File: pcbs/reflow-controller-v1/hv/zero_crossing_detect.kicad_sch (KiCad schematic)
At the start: 13 parts, among them Q1601 MMBT3904, Q1602 140357145200

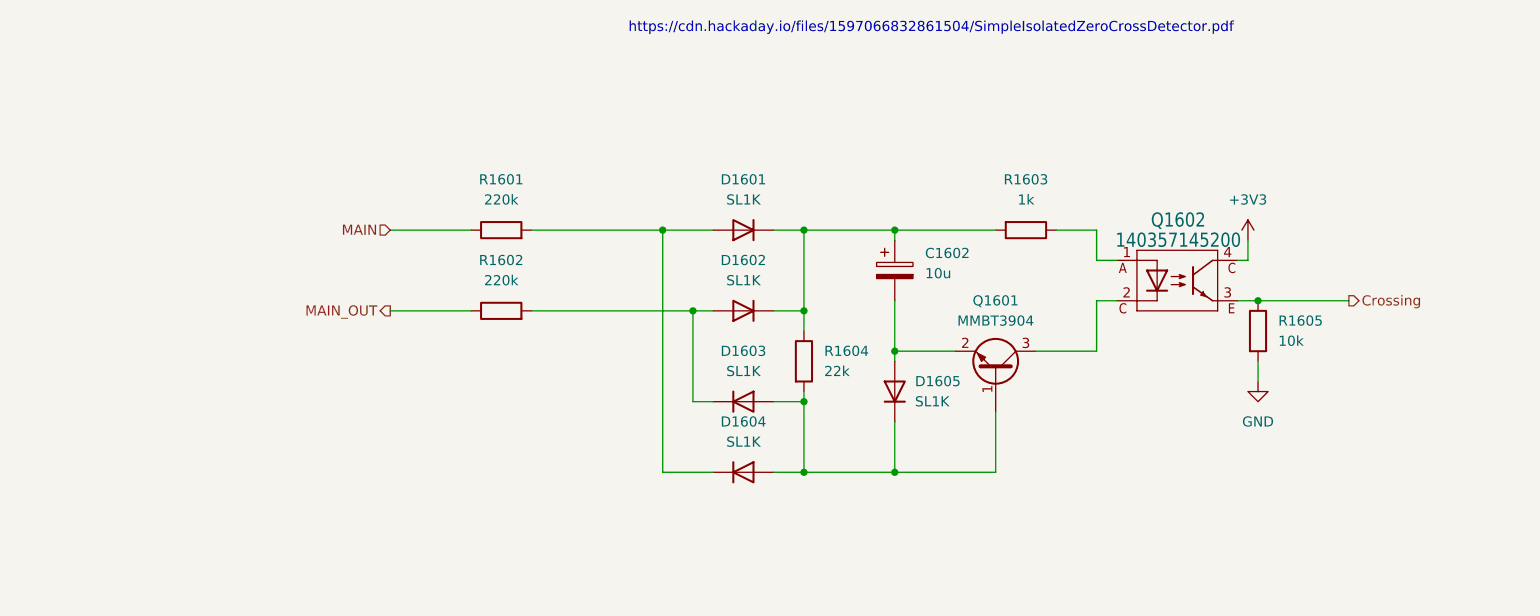
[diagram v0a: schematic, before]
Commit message: split pcbs into two for safety
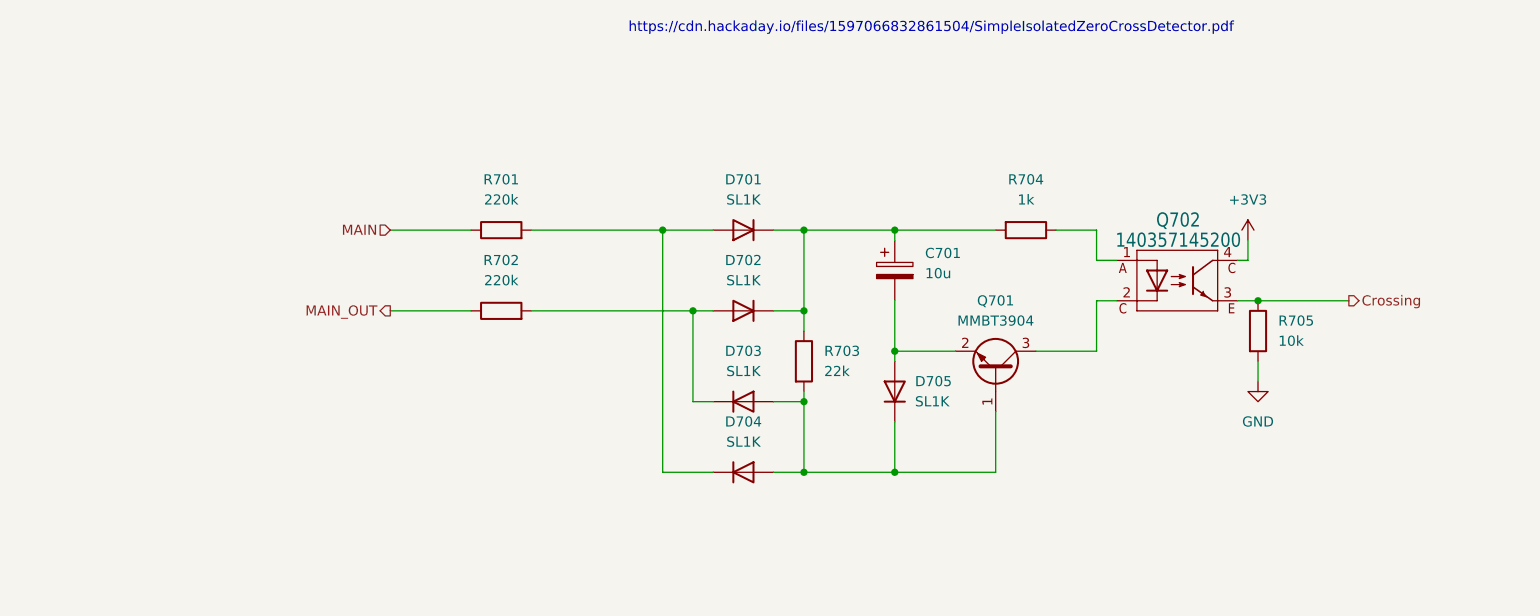
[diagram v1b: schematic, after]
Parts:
- Q702: renamed from Q1602; footprint WL-OCPT_LSOP4 -> wuerth:WL-OCPT_SOP4
- renumbered C1602 to C701, D1601 to D701, D1602 to D702, D1603 to D703, D1604 to D704, D1605 to D705, Q1601 to Q701, R1601 to R701, R1602 to R702, R1604 to R703, R1603 to R704, R1605 to R705

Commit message: Initial hv placing
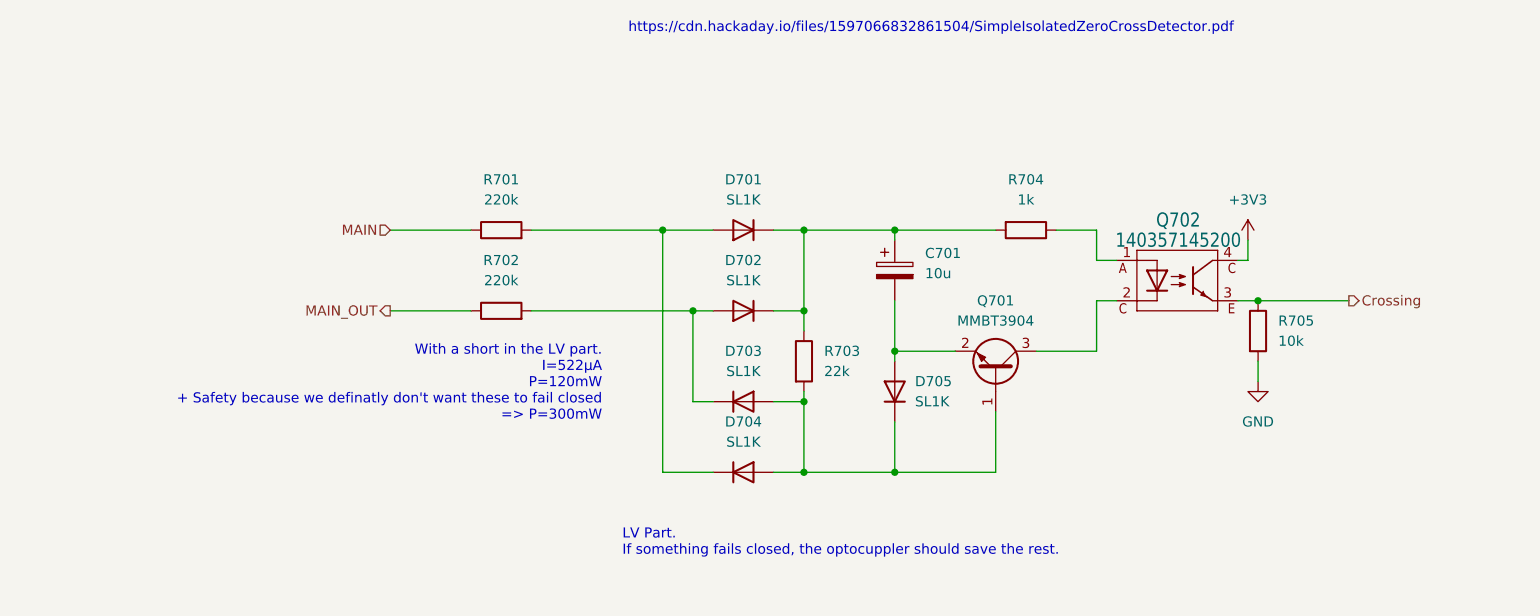
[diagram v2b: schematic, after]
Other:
- note added: "LV Part. If something fails closed, the optocuppler should save the rest."
- note added: "With a short in the LV part. I=522μA P=120mW + Safety because we definatly don't want these to fail closed => P=300mW"
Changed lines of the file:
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@@
+		)
+	)
+	(text "LV Part. \nIf something fails closed, the optocuppler should save the rest.\n"
+		(exclude_from_sim no)
+		(at 78.74 81.28 0)
+		(effects
+			(font
+				(size 1.27 1.27)
+			)
+			(justify left)
+		)
+	)
+	(text "With a short in the LV part.\nI=522μA\nP=120mW\n+ Safety because we definatly don't want these to fail closed\n=> P=300mW\n"
+		(exclude_from_sim no)
+		(at 76.2 61.214 0)
+		(effects
+			(font
+				(size 1.27 1.27)
+			)
+			(justify right)
 		)
 	)
@@
 		)
 	)
+	(rule_area
+		(polyline
+			(pts
+				(xy 78.74 33.02) (xy 78.74 77.47) (xy 137.16 77.47) (xy 137.16 33.02)
+			)
+			(stroke
+				(width 0)
+				(type dash)
+			)
+			(fill
+				(type none)
+			)
+		)
+	)
+	(netclass_flag ""
+		(length 2.54)
+		(shape round)
+		(at 97.79 33.02 0)
+		(fields_autoplaced yes)
+		(effects
+			(font
+				(size 1.27 1.27)
+			)
+			(justify left bottom)
+		)
+		(property "Netclass" "LV"
+			(at 98.4885 30.48 0)
+			(effects
+				(font
+					(size 1.27 1.27)
+				)
+				(justify left)
+			)
+		)
+		(property "Component Class" ""
+			(at -46.99 0 0)
+			(effects
+				(font
+					(size 1.27 1.27)
+					(italic yes)
+				)
+			)
+		)
+	)

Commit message: improve component selection
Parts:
- removed D702, D703, D704, D705: SL1K, Diode_SMD:D_SOD-123F, symbol Device:D
- added D706: BAS3007A-RPP, Package_TO_SOT_SMD:SOT-143, symbol Diode_Bridge:B40C2300-1500A
- C701: Order (none) -> Würth 865230440002
- D701: value SL1K -> BAS21J; footprint Diode_SMD:D_SOD-123F -> Diode_SMD:D_SOD-323F
- R701, R702: Order (none) -> Würth 560112132017
- R703, R704, R705: footprint Resistor_SMD:R_0603_1608Metric -> Resistor_SMD:R_0402_1005Metric
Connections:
- net at R702.2: now also D706.2
- net at C701.1, R703.1, R704.2: now also D706.4 (+); no longer D701.1 (K)
- net at Q701.1 (B), R703.2: now also D701.1 (K), D706.1 (-)
- net at C701.2, Q701.2 (E): now also D701.2 (A)
- net at R701.2: now also D706.3; no longer D701.2 (A)
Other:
- note added: "With just the voltage devider Resistors I=497μA P=110μW + Safety because we definatly don't want these to fail closed => P=200mW Per Resistor 5% Smaller values result in ~524μA 5% Tollerance should be fine"
- note removed: "With a short in the LV part. I=522μA P=120mW + Safety because we definatly don't want these to fail closed => P=300mW"
- moved on the sheet: C701, Q701, Q702, R701, R702, R703, R704, R705

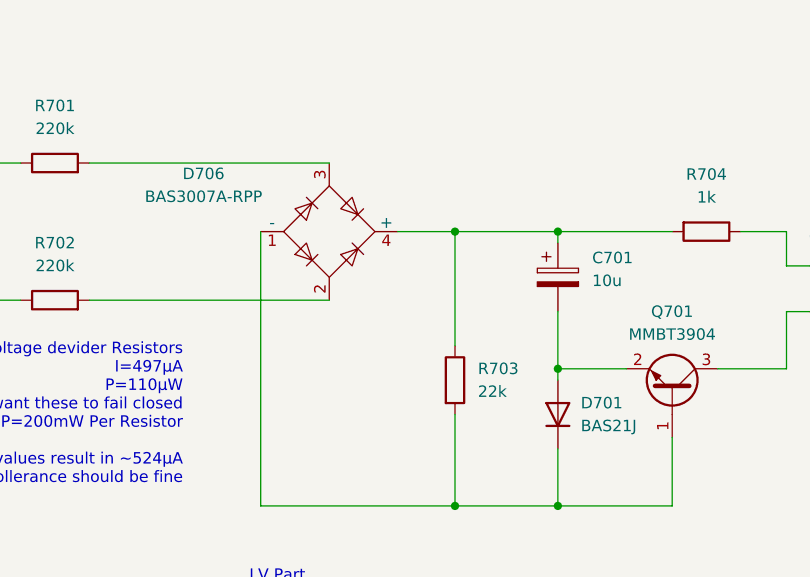
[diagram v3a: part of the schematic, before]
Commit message: route hv pcb
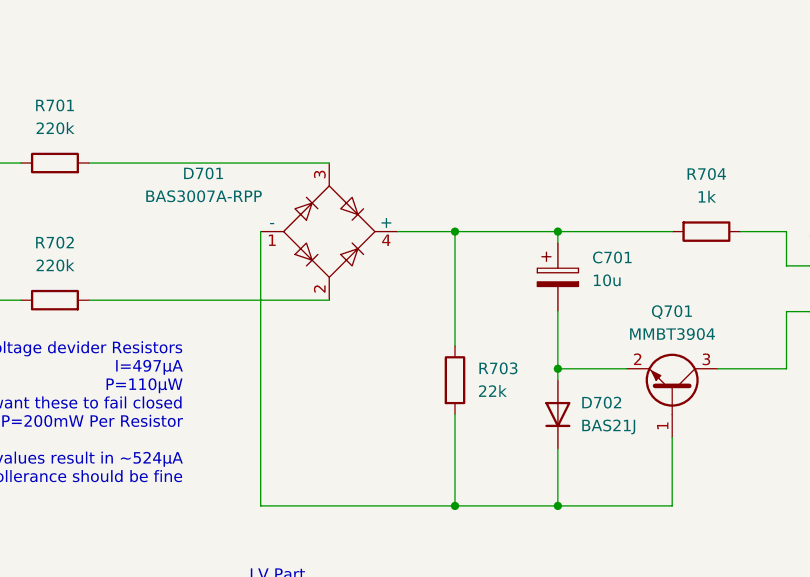
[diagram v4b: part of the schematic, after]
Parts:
- renumbered D706 to D701, D701 to D702
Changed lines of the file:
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@@
 		(dnp no)
 		(fields_autoplaced yes)
-		(property "Reference" "D701"
+		(property "Reference" "D702"
 			(at 125.73 66.0399 90)
 			(effects
@@
 			(project ""
 				(path "/bfc257b6-4a03-4e6b-b2e0-eeb653e202b4/9b322a1f-f97f-4e42-b612-e764afdaf494"
-					(reference "D701")
+					(reference "D702")
 					(unit 1)
 				)
@@
 		(on_board yes)
 		(dnp no)
-		(property "Reference" "D706"
+		(property "Reference" "D701"
 			(at 83.82 40.5698 0)
 			(effects
@@
 			(project ""
 				(path "/bfc257b6-4a03-4e6b-b2e0-eeb653e202b4/9b322a1f-f97f-4e42-b612-e764afdaf494"
-					(reference "D706")
-					(unit 1)
-				)
+					(reference "D701")
+					(unit 1)
+				)
